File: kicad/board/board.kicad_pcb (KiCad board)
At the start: 4 copper layers, 58.7 x 74.9 mm, 50 parts, among them J1 i2c_connector, J2 uart_connector, J3 spi_connector, J4 debug header, J5 powerheader, J6 USB_B_Micro, J7 gpioheader A, J8 gpioheader B, SW1 reset button, U1 BQ24075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

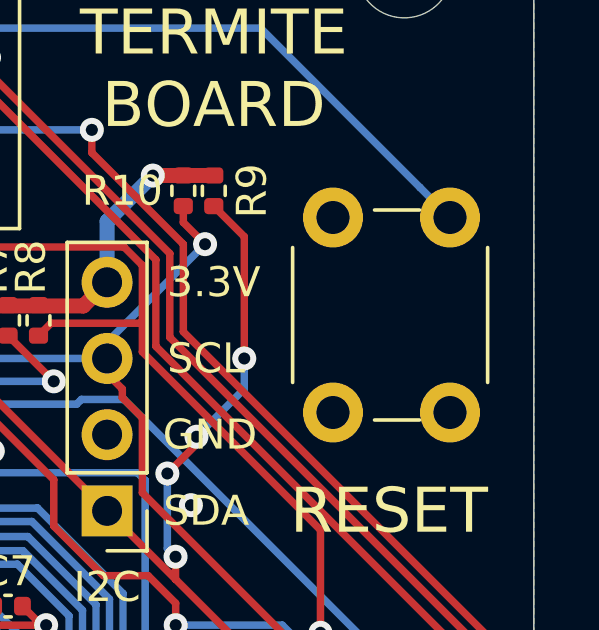
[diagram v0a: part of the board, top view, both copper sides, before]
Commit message: fixing #6
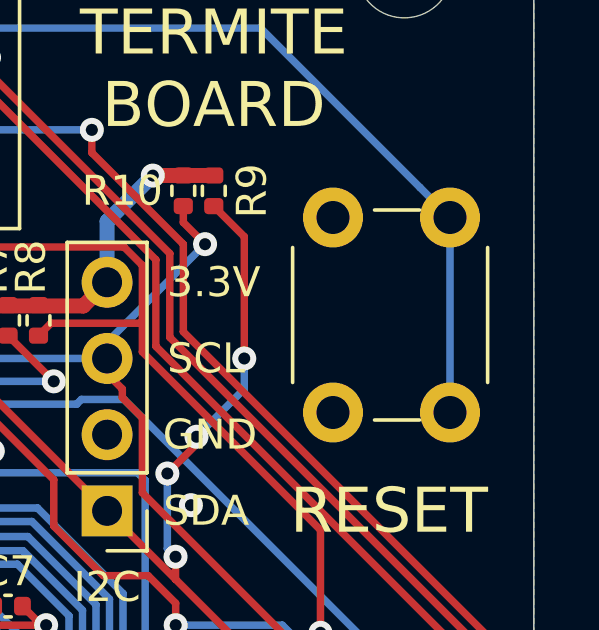
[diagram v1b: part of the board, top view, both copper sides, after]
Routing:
- net /rst: track 77.6 -> 84.1 mm

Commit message: v1.1 adding
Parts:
- added D2: red_led, LED_SMD:LED_0603_1608Metric, F.Cu at (41.4, 57.5)
- added D3: green_led, LED_SMD:LED_0603_1608Metric, F.Cu at (39.8, 57.5)
- added R11: 3.0K, Resistor_SMD:R_0603_1608Metric_Pad0.98x0.95mm_HandSolder, F.Cu at (39.0, 65.5)
- added R12: 150, Resistor_SMD:R_0402_1005Metric, F.Cu at (37.0, 62.9)
- added R13: 100, Resistor_SMD:R_0402_1005Metric, F.Cu at (36.0, 62.9)
- added R14: 10kΩ, Resistor_SMD:R_0402_1005Metric, F.Cu at (40.1, 78.3)
- added R15: 10kΩ, Resistor_SMD:R_0402_1005Metric, F.Cu at (41.3, 78.3)
- added SW2: pw_sw, components:K301235D, F.Cu at (75.0, 68.8)
- added TP3: batvoltage, TestPoint:TestPoint_Pad_D1.0mm, F.Cu at (26.1, 65.9)
- R1: value 1.13kΩ -> 1.8kΩ; footprint Resistor_SMD:R_0402_1005Metric -> Resistor_SMD:R_0603_1608Metric_Pad0.98x0.95mm_HandSolder
- TP1, TP2: footprint TestPoint:TestPoint_Pad_D2.0mm -> TestPoint:TestPoint_Pad_D1.0mm
- moved R10 20.7 mm to (70.6, 87.9), turned to 315 degrees
- moved R9 20.0 mm to (71.4, 87.2), turned to 135 degrees
- moved D1 19.7 mm to (57.3, 89.8), turned to 180 degrees
- moved TP2 16.9 mm to (57.0, 72.5)
- moved C3 16.7 mm to (63.5, 78.9), turned to 45 degrees
- moved R4 16.3 mm to (53.9, 90.8), turned to 180 degrees
- moved C11 16.1 mm to (63.0, 81.5), turned to 225 degrees
- moved R3 15.5 mm to (53.9, 89.7), turned to 180 degrees
- moved R5 14.9 mm to (55.1, 88.1), turned to 270 degrees
- moved U4 13.6 mm to (68.8, 73.0), turned to 270 degrees
- moved J1 13.5 mm to (75.5, 85.4)
- moved C14 13.3 mm to (72.5, 75.2), turned to 180 degrees
- moved R7 12.6 mm to (72.5, 76.2), turned to 180 degrees
- moved C6 12.3 mm to (50.9, 79.1), turned to 135 degrees
- moved R8 11.1 mm to (72.5, 74.2), turned to 0 degrees
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- renumbered BT1 to BAT
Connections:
- J3 pad 1: /spi_sclk -> /spi_cs
- J3 pad 2: /spi_mosi -> /spi_sclk
- J3 pad 4: /spi_cs -> /spi_mosi
- J5 pad 1: /RGB_G -> /RGB_B
- J5 pad 3: /RGB_B -> /RGB_G
- J7 pad 1: /pb0 -> /pb13
- J7 pad 10: /pa3 -> /uart_rx
- J7 pad 11: /eeprom_sda -> /pb4
- J7 pad 12: /pa2 -> +3V3
- J7 pad 13: /eeprom_scl -> /pb5
- J7 pad 14: /pa1 -> GND
- J7 pad 15: /boot1 -> /pb6
- J7 pad 16: /pa0 -> /swdio
- J7 pad 2: /spi_mosi -> /pb14
- J7 pad 3: /pb1 -> /pb12
- J7 pad 4: /spi_miso -> /pb15
- J7 pad 5: /pb14 -> /swclk
- J7 pad 6: /spi_sclk -> /pa8
- J7 pad 7: /pb13 -> /pa15
- J7 pad 8: /spi_cs -> /uart_tx
- J7 pad 9: /pb12 -> /pb3
- J8 pad 1: /pb3 -> /spi_sclk
- J8 pad 10: /usb_d- -> /pa0
- J8 pad 11: /pa8 -> /boot1
- J8 pad 12: /uart_rx -> /i2c_sda
- J8 pad 13: /i2c_sda -> /eeprom_scl
- J8 pad 14: /uart_tx -> /i2c_scl
- J8 pad 15: /i2c_scl -> /eeprom_sda
- J8 pad 16: /pb15 -> /pb7
- J8 pad 2: /pa15 -> /spi_cs
- J8 pad 3: /pb4 -> /spi_miso
- J8 pad 4: /swclk -> /pa3
- J8 pad 5: /pb5 -> /spi_mosi
- J8 pad 6: /swdio -> /pa2
- J8 pad 7: /pb6 -> /pb0
- J8 pad 8: /usb_d+ -> /pa1
- J8 pad 9: /pb7 -> /pb1
- JP1 pad 2: /boot0 -> Net-(JP1-Pad2)
- JP2 pad 2: /boot1 -> Net-(JP2-Pad2)
- U3 pad 3: Net-(C12-Pad2) -> Net-(SW2-Pad2)
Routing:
- net +3V3: track 145.3 -> 45.7 mm, vias 6 -> 9
- net Net-(SW2-Pad2): track 0.00 -> 58.8 mm, vias 0 -> 1
- net Net-(C12-Pad2): track 21.7 -> 73.1 mm, vias 0 -> 1
- net /usb_d-: track 69.5 -> 25.7 mm, vias 2 -> 0
- net /uart_rx: track 115.4 -> 75.1 mm, vias 3 -> 1
- net /usb_d+: track 69.9 -> 29.7 mm, vias 2 -> 0
- net /eeprom_scl: track 101.7 -> 63.0 mm, vias 5 -> 2
- net /rst: track 84.1 -> 49.8 mm, vias 2 -> 1
- net /uart_tx: track 105.8 -> 72.5 mm
- net /spi_mosi: track 52.8 -> 78.8 mm, vias 0 -> 3
- net /swdio: track 108.5 -> 83.4 mm, vias 2 -> 1
- net /eeprom_sda: track 87.6 -> 62.6 mm, vias 5 -> 1
- net +5V: track 59.9 -> 35.2 mm, vias 5 -> 7
- net /pa0: track 55.0 -> 30.5 mm, vias 0 -> 1
- net /boot1: track 89.5 -> 66.4 mm, vias 1 -> 3
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- added copper zone on In2.Cu, net +5V
- removed copper zone on In2.Cu, net GND
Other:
- net class Default: clearance 0.2 -> 0.199
- rule trace_clearance: 0.2 -> 0.199
- board text added: "Docs and more: github.com/CvRXX/termite"
- board text added: "PWR"
- board text added: "RGB.G"
- board text added: "V1.01"
- board text removed: "PA11"
- board text removed: "PA12"
- board text removed: "V1.00"

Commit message: putting the thermistor replacement resistor to gnd instead of 5v fixing #18
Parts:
- renumbered BAT to BT1
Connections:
- R2 pad 2: +5V -> GND
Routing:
- net GND: track 60.6 -> 61.7 mm, vias 24 -> 25
- net +5V: track 35.2 -> 34.1 mm, vias 7 -> 6
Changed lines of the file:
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@@
-(kicad_pcb (version 20171130) (host pcbnew 5.1.8)
+(kicad_pcb (version 20171130) (host pcbnew 5.1.9)
   (general
     (thickness 1.6)
@@
     (descr "Through hole straight pin header, 1x02, 2.54mm pitch, single row")
     (tags "Through hole pin header THT 1x02 2.54mm single row")
-    (fp_text reference BAT (at 0 -2.33) (layer F.SilkS)
+    (fp_text reference BT1 (at 0 -2.33) (layer F.SilkS)
       (effects (font (size 1 1) (thickness 0.15)))
     )
@@
     )
     (pad 2 smd roundrect (at 0.51 0 90) (size 0.54 0.64) (layers F.Cu F.Paste F.Mask) (roundrect_rratio 0.25)
-      (net 6 +5V))
+      (net 2 GND))
     (pad 1 smd roundrect (at -0.51 0 90) (size 0.54 0.64) (layers F.Cu F.Paste F.Mask) (roundrect_rratio 0.25)
       (net 52 "Net-(R2-Pad1)"))
@@
   (segment (start 36.322 85.344) (end 35.825 84.847) (width 0.5) (layer B.Cu) (net 6))
   (segment (start 37.9 68.35) (end 37.825 68.35) (width 0.25) (layer F.Cu) (net 6))
-  (segment (start 33.985 62.365) (end 33.85 62.5) (width 0.25) (layer F.Cu) (net 6))
-  (segment (start 34.9 62.365) (end 33.985 62.365) (width 0.25) (layer F.Cu) (net 6))
-  (via (at 33.85 62.5) (size 0.8) (drill 0.4) (layers F.Cu B.Cu) (net 6))
+  (segment (start 33.985 62.365) (end 33.85 62.5) (width 0.25) (layer F.Cu) (net 2))
+  (segment (start 34.9 62.365) (end 33.985 62.365) (width 0.25) (layer F.Cu) (net 2))
+  (via (at 33.85 62.5) (size 0.8) (drill 0.4) (layers F.Cu B.Cu) (net 2))
   (segment (start 36.47549 68.35) (end 35.7525 67.62701) (width 0.5) (layer F.Cu) (net 6))
   (segment (start 37.9 68.35) (end 36.47549 68.35) (width 0.5) (layer F.Cu) (net 6))

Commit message: adding labeling for uart fixing #12
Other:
- board text added: "3.3v"
- board text added: "NC"
- board text added: "RX"
- board text added: "TX"
- board text added: "rst"
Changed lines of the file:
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@@
   (general
     (thickness 1.6)
-    (drawings 69)
+    (drawings 75)
     (tracks 845)
     (zones 0)
@@
     )
   )
+  (gr_text NC (at 44.2 60.25 90) (layer B.SilkS)
+    (effects (font (size 1 1) (thickness 0.15)) (justify mirror))
+  )
+  (gr_text GND (at 46.8 60.25 90) (layer B.SilkS)
+    (effects (font (size 1 1) (thickness 0.15)) (justify mirror))
+  )
+  (gr_text RX (at 49.2 60.25 90) (layer B.SilkS)
+    (effects (font (size 1 1) (thickness 0.15)) (justify mirror))
+  )
+  (gr_text TX (at 51.8 60.25 90) (layer B.SilkS)
+    (effects (font (size 1 1) (thickness 0.15)) (justify mirror))
+  )
+  (gr_text rst (at 54.4 60.25 90) (layer B.SilkS)
+    (effects (font (size 1 1) (thickness 0.15)) (justify mirror))
+  )
+  (gr_text 3.3v (at 56.9 60.25 90) (layer B.SilkS)
+    (effects (font (size 1 1) (thickness 0.15)) (justify mirror))
+  )
   (gr_text PWR (at 71.425 66.2 90) (layer F.SilkS)

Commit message: adding labeling for the power switch
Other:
- board text added: "ON"
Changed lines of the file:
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@@
   (general
     (thickness 1.6)
-    (drawings 75)
+    (drawings 76)
     (tracks 845)
     (zones 0)
@@
     )
   )
+  (gr_text ON (at 75.1 63.2) (layer F.SilkS)
+    (effects (font (size 1 1) (thickness 0.2)))
+  )
   (gr_text NC (at 44.2 60.25 90) (layer B.SilkS)

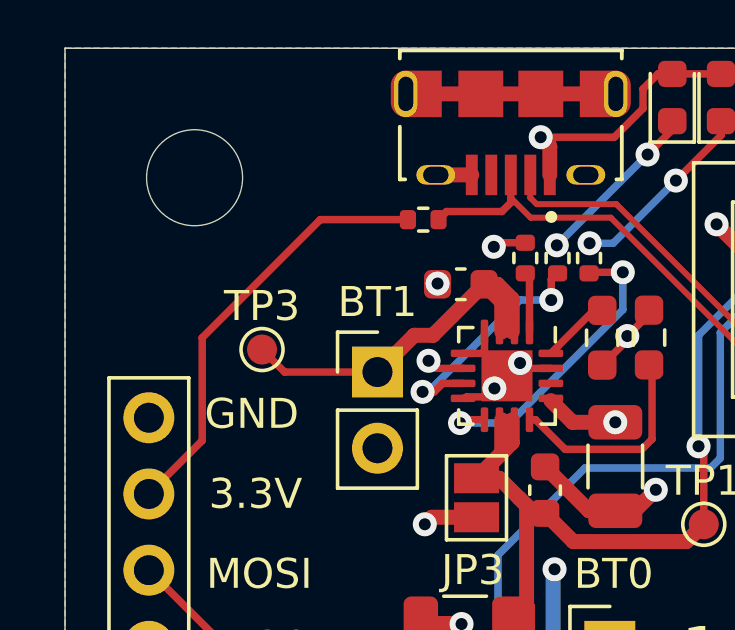
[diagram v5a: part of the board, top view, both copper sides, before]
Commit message: adding polarity marking for bat connector fixing #14
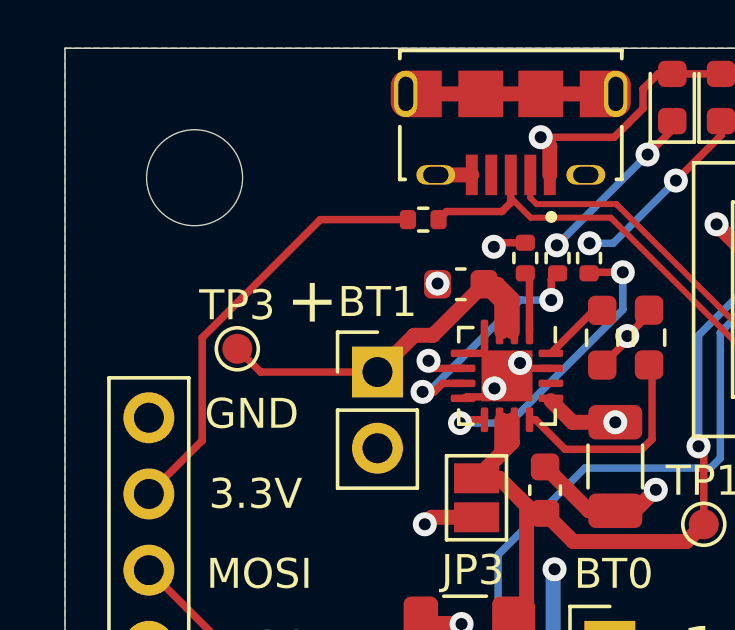
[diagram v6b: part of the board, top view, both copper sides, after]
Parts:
- moved TP3 0.83 mm to (25.3, 65.9)
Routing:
- net Net-(BT1-Pad1): track 13.0 -> 13.8 mm
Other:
- board text added: "+"
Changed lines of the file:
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@@
   (general
     (thickness 1.6)
-    (drawings 76)
+    (drawings 78)
     (tracks 845)
     (zones 0)
@@
   )
   (module TestPoint:TestPoint_Pad_D1.0mm (layer F.Cu)
-    (at 26.125 65.925)
+    (at 25.3 65.9)
     (descr "SMD pad as test Point, diameter 1.0mm")
     (tags "test point SMD pad")
@@
     )
   )
+  (gr_text + (at 27.8 64.3) (layer B.SilkS)
+    (effects (font (size 1.5 1.5) (thickness 0.3)))
+  )
+  (gr_text + (at 27.8 64.3) (layer F.SilkS)
+    (effects (font (size 1.5 1.5) (thickness 0.3)))
+  )
   (gr_text ON (at 75.1 63.2) (layer F.SilkS)
     (effects (font (size 1 1) (thickness 0.2)))
@@
   (gr_line (start 78.232 55.88) (end 19.558 55.88) (layer Edge.Cuts) (width 0.05))
   (gr_line (start 78.232 130.81) (end 78.232 55.88) (layer Edge.Cuts) (width 0.05))
-  (segment (start 26.875 66.675) (end 26.125 65.925) (width 0.25) (layer F.Cu) (net 1))
-  (segment (start 29.972 66.675) (end 26.875 66.675) (width 0.25) (layer F.Cu) (net 1))
   (segment (start 34.11501 64.34001) (end 34.11501 65.3395) (width 0.5) (layer F.Cu) (net 1))
   (segment (start 33.525 63.75) (end 34.11501 64.34001) (width 0.5) (layer F.Cu) (net 1))
@@
   (segment (start 31.197162 65.449838) (end 29.972 66.675) (width 0.5) (layer F.Cu) (net 1))
   (segment (start 33.525 63.75) (end 31.825162 65.449838) (width 0.5) (layer F.Cu) (net 1))
+  (segment (start 26.075 66.675) (end 25.3 65.9) (width 0.25) (layer F.Cu) (net 1))
+  (segment (start 29.972 66.675) (end 26.075 66.675) (width 0.25) (layer F.Cu) (net 1))
   (segment (start 59.376504 73.382316) (end 59.376504 72.860955) (width 0.25) (layer F.Cu) (net 2))
   (via (at 59.376504 72.860955) (size 0.8) (drill 0.4) (layers F.Cu B.Cu) (net 2))
